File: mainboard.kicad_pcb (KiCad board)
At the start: 2 copper layers, 64.8 x 50.8 mm, 25 parts, among them J1 105017-1001, J2 XT60-M, Q1 AOD4184A, Q2 AOD4184A, U1 ESP32-WROOM-32E_(16MB), U2 CH340E, U3 AMS1117-3.3, U4 PAM8403DR

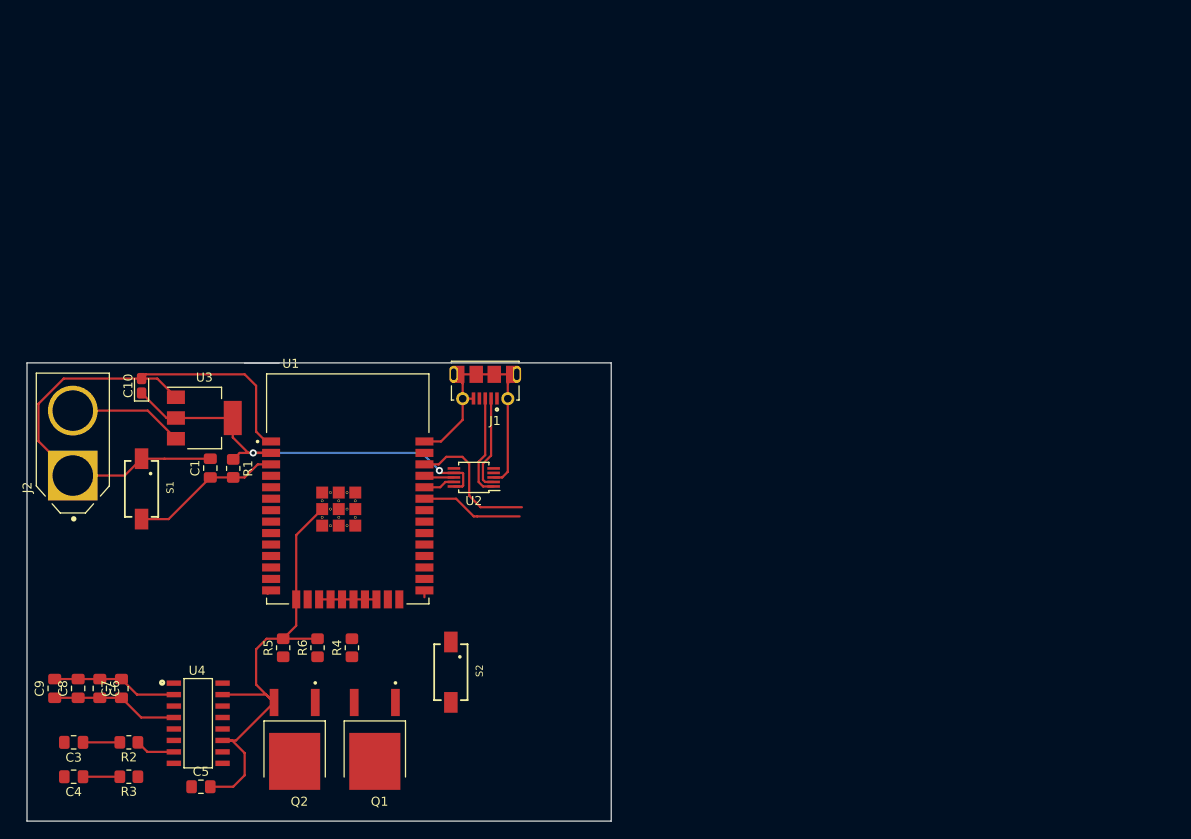
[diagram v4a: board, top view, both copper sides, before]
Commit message: PCB herwerkt na feedback
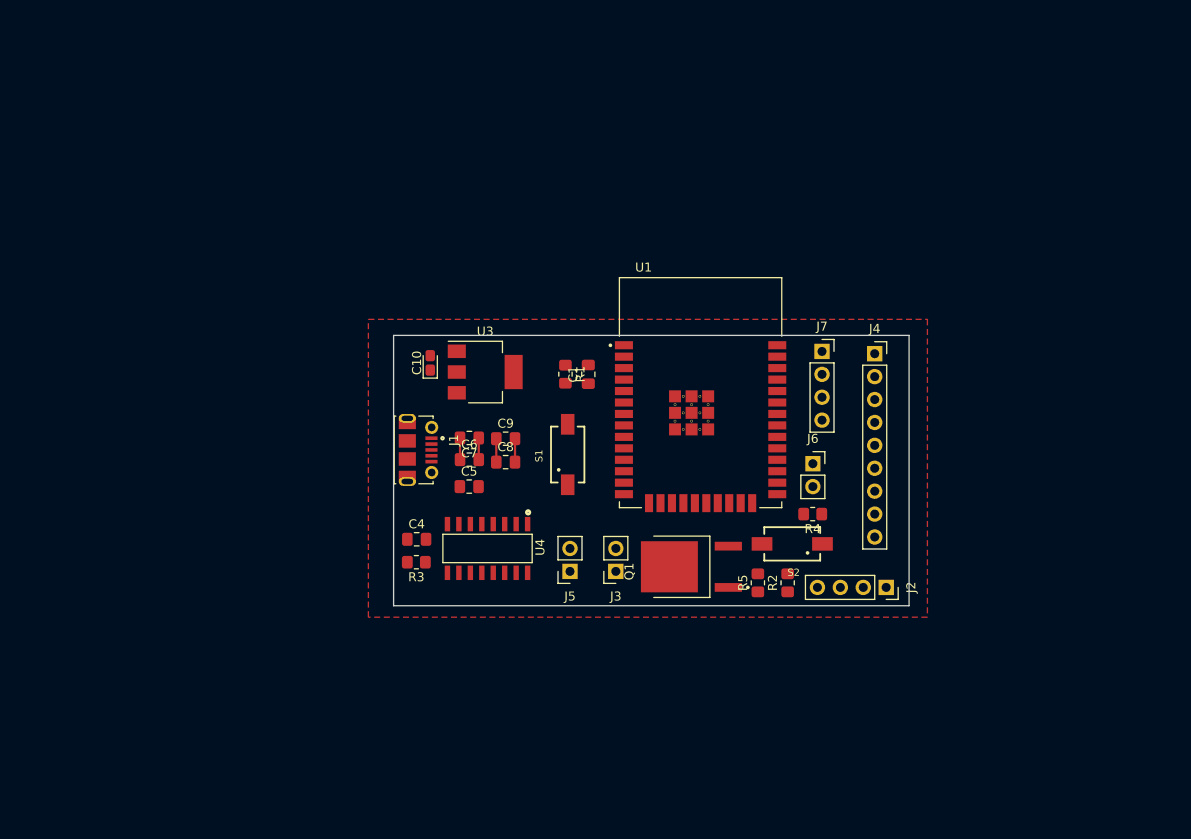
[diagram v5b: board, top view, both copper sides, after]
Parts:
- removed C3: C, Capacitor_SMD:C_0805_2012Metric_Pad1.18x1.45mm_HandSolder
- removed Q2: AOD4184A, mylibs:DPAK228P994X240-4N
- removed R6: R, Resistor_SMD:R_0805_2012Metric_Pad1.20x1.40mm_HandSolder
- removed U2: CH340E, Package_SO:MSOP-10_3x3mm_P0.5mm
- added J3: Conn_01x02_Female, Connector_PinSocket_2.54mm:PinSocket_1x02_P2.54mm_Vertical, F.Cu at (104.6, 109.5)
- added J4: Conn_01x09_Female, Connector_PinSocket_2.54mm:PinSocket_1x09_P2.54mm_Vertical, F.Cu at (133.3, 85.3)
- added J5: Conn_01x02_Female, Connector_PinSocket_2.54mm:PinSocket_1x02_P2.54mm_Vertical, F.Cu at (99.6, 109.5)
- added J6: Conn_01x02_Female, Connector_PinSocket_2.54mm:PinSocket_1x02_P2.54mm_Vertical, F.Cu at (126.5, 97.5)
- added J7: Conn_01x04_Female, Connector_PinSocket_2.54mm:PinSocket_1x04_P2.54mm_Vertical, F.Cu at (127.5, 85.1)
- J2: value XT60-M -> Conn_01x04_Female; footprint mylibs:AMASS_XT60-M -> Connector_PinSocket_2.54mm:PinSocket_1x04_P2.54mm_Vertical
- moved J2 91.6 mm to (134.6, 111.3), turned to 270 degrees
- moved R2 75.1 mm to (123.7, 110.7), turned to 90 degrees
- moved C9 57.1 mm to (92.4, 94.8), turned to 0 degrees
- moved C8 53.6 mm to (92.4, 97.4), turned to 0 degrees
- moved R4 53.2 mm to (126.5, 103.1), turned to 180 degrees
- moved R5 53.1 mm to (120.4, 110.7)
- moved C6 48.2 mm to (88.4, 97.1), turned to 0 degrees
- moved C7 47.5 mm to (88.4, 94.7), turned to 180 degrees
- moved S1 47.4 mm to (99.3, 96.5), turned to 90 degrees
- moved C4 46.2 mm to (82.6, 105.9), turned to 0 degrees
- moved C5 44.6 mm to (88.4, 100.1)
- moved C1 43.2 mm to (101.6, 87.6)
- moved U1 40.5 mm to (114.0, 89.7)
- moved S2 40.4 mm to (124.2, 106.4), turned to 180 degrees
- moved Q1 40.0 mm to (113.0, 109.0), turned to 90 degrees
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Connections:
- net +OUT_L renamed Net-(U4-Pad1)
- net -OUT_L renamed Net-(U4-Pad3)
- net Net-(U1-Pad7) renamed IRB
- J1 pad 1: Net-(J1-Pad1) -> 5V
- J2 pad 1: GND -> RXD
- J2 pad 2: Net-(J2-Pad2) -> TXD
- Q1 pad 1: Net-(Q1-Pad1) -> Mosfet_Trig
- R2 pad 1: Net-(R2-Pad1) -> 3V3
- R2 pad 2: Net-(C3-Pad1) -> TXD
- R4 pad 1: Net-(Q1-Pad1) -> 3V3
- R4 pad 2: Mosfet_Trig -> Net-(R4-Pad2)
- R5 pad 1: Net-(Q1-Pad1) -> Mosfet_Trig
- S2 pad 1: Net-(S2-Pad1) -> Net-(R4-Pad2)
- U1 pad 10: Net-(U1-Pad10) -> TFT_CS
- U1 pad 11: Net-(U1-Pad11) -> INR
- U1 pad 12: Net-(U1-Pad12) -> TFT_DC
- U1 pad 14: SHND -> Net-(U1-Pad14)
- U1 pad 25: Net-(S2-Pad1) -> Net-(R4-Pad2)
- U1 pad 26: Net-(U1-Pad26) -> PN532_IRQ
- U1 pad 29: Net-(U1-Pad29) -> PN532_RESET
- U1 pad 30: Net-(U1-Pad30) -> TFT_CLK
- U1 pad 31: Net-(U1-Pad31) -> TFT_MISO
- U1 pad 33: Net-(U1-Pad33) -> SDA
- U1 pad 36: Net-(U1-Pad36) -> SCL
- U1 pad 37: Net-(U1-Pad37) -> TFT_MOSI
- U1 pad 8: Net-(U1-Pad8) -> TFT_RST
- U1 pad 9: Net-(U1-Pad9) -> SHND
- U3 pad 3: Net-(J2-Pad2) -> 5V
- U4 pad 7: Net-(R2-Pad1) -> Net-(U4-Pad7)
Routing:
- net GND: track 165.5 -> 5.00 mm
- net 3V3: track 49.5 -> 0.00 mm, vias 2 -> 0
- net Net-(C1-Pad1): track 16.9 -> 0.00 mm
- net Net-(U1-Pad36): track 15.5 -> 0.00 mm
- net Net-(J2-Pad2): track 12.7 -> 0.00 mm
- net Net-(J1-Pad3): track 11.4 -> 0.00 mm
- net Net-(U1-Pad33): track 11.4 -> 0.00 mm
- net Net-(J1-Pad2): track 10.7 -> 0.00 mm
- net 5V: track 14.1 -> 5.00 mm
- net Net-(U1-Pad17): track 6.35 -> 0.00 mm
- net Net-(R2-Pad1): track 4.43 -> 0.00 mm
- net Net-(C4-Pad1): track 4.08 -> 0.00 mm
- net Net-(C3-Pad1): track 4.08 -> 0.00 mm
- net RXD: track 3.51 -> 0.00 mm
- net TXD: track 3.34 -> 0.00 mm
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- added copper zone on F.Cu, net GND
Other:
- board size 64.8 x 50.8 mm -> 57.1 x 30 mm
- board text removed: "PWM"
- board text removed: "Ruimte voor connectors"
- board text removed: "belangrijke IO pinnen"

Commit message: beetje tracing gedaan
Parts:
- moved S1 0.46 mm to (98.9, 96.3)
- moved C8 0.29 mm to (92.5, 97.1)
- moved C10 0.22 mm to (84.1, 86.6)
- moved R1 0.16 mm to (98.9, 87.7)
- moved C9 0.08 mm to (92.5, 94.7)
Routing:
- net 5V: track 5.00 -> 33.9 mm
- net INR: track 0.00 -> 27.5 mm
- net 3V3: track 0.00 -> 23.9 mm
- net GND: track 5.00 -> 22.7 mm
- net Net-(C1-Pad1): track 0.00 -> 12.2 mm
- net -OUT_R: track 0.00 -> 11.6 mm
- net Net-(R3-Pad1): track 0.00 -> 7.98 mm
- net +OUT_R: track 0.00 -> 6.63 mm
- net Net-(C5-Pad1): track 0.00 -> 4.73 mm
- net Net-(C4-Pad1): track 0.00 -> 2.54 mm

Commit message: sorry stef pt. 3
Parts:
- moved J6 0.80 mm to (127.3, 97.3)
- moved J7 0.57 mm to (127.3, 85.6)
- moved J4 0.25 mm to (133.3, 85.6)

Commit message: tis fokking mooi wtf
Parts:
- removed C10: CP, Capacitor_Tantalum_SMD:CP_EIA-1608-08_AVX-J_Pad1.25x1.05mm_HandSolder
- added C2: 100n, Capacitor_SMD:C_0805_2012Metric_Pad1.18x1.45mm_HandSolder, F.Cu at (99.1, 88.9)
- added C3: 22u, Capacitor_SMD:C_0805_2012Metric_Pad1.18x1.45mm_HandSolder, F.Cu at (83.8, 86.4)
- added R6: 10K, Resistor_SMD:R_0805_2012Metric_Pad1.20x1.40mm_HandSolder, F.Cu at (125.7, 97.8)
- added R7: 10K, Resistor_SMD:R_0805_2012Metric_Pad1.20x1.40mm_HandSolder, F.Cu at (102.9, 95.2)
- C1: value C -> 100n
- C4: value C -> 0.47u
- C5: value C -> 0.1u
- C6, C7, C9: value C -> 1u
- C8: value C -> 470u
- R1, R2, R3, R4, R5: value R -> 10K
- moved J6 8.77 mm to (132.7, 104.1)
- moved J4 6.60 mm to (139.1, 88.9)
- moved J7 4.85 mm to (132.1, 85.1)
- moved R1 2.68 mm to (96.5, 88.9)
- moved J1 2.54 mm to (79.0, 96.0)
- moved C1 1.27 mm to (101.6, 88.9)
- moved R3 1.27 mm to (81.3, 108.5)
- moved C4 1.27 mm to (81.3, 105.9)
- moved R2 0.13 mm to (123.8, 110.7), turned to 270 degrees
- turned C6 to 180 degrees
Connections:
- C6 pad 1: GND -> 5V
- C6 pad 2: 5V -> GND
- J4 pad 3: TFT_CS -> TFT_RST
- J4 pad 4: TFT_RST -> TFT_CS
- J4 pad 7: TFT_CLK -> TFT_MISO
- J4 pad 8: 3V3 -> TFT_CLK
- J4 pad 9: TFT_MISO -> 3V3
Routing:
- net 3V3: track 23.9 -> 112.9 mm, vias 0 -> 1
- net TXD: track 0.00 -> 43.5 mm, vias 0 -> 2
- net SHND: track 0.00 -> 39.2 mm, vias 0 -> 2
- net TFT_RST: track 0.00 -> 35.3 mm, vias 0 -> 1
- net TFT_DC: track 0.00 -> 33.8 mm, vias 0 -> 1
- net TFT_CS: track 0.00 -> 33.8 mm, vias 0 -> 1
- net RXD: track 0.00 -> 33.3 mm, vias 0 -> 1
- net 5V: track 33.9 -> 64.6 mm, vias 0 -> 2
- net TFT_MOSI: track 0.00 -> 26.1 mm
- net TFT_CLK: track 0.00 -> 21.5 mm
- net TFT_MISO: track 0.00 -> 21.0 mm
- net Mosfet_Trig: track 0.00 -> 16.1 mm, vias 0 -> 2
- net PN532_RESET: track 0.00 -> 13.8 mm
- net PN532_IRQ: track 0.00 -> 13.1 mm, vias 0 -> 1
- net SCL: track 0.00 -> 10.9 mm, vias 0 -> 1
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- added copper zone on F.Cu, net (none)
- added copper zone on B.Cu, net GND
- removed copper zone on F.Cu, net GND
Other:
- board size 57.1 x 30 mm -> 66 x 33.7 mm
